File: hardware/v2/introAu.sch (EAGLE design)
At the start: 21 parts

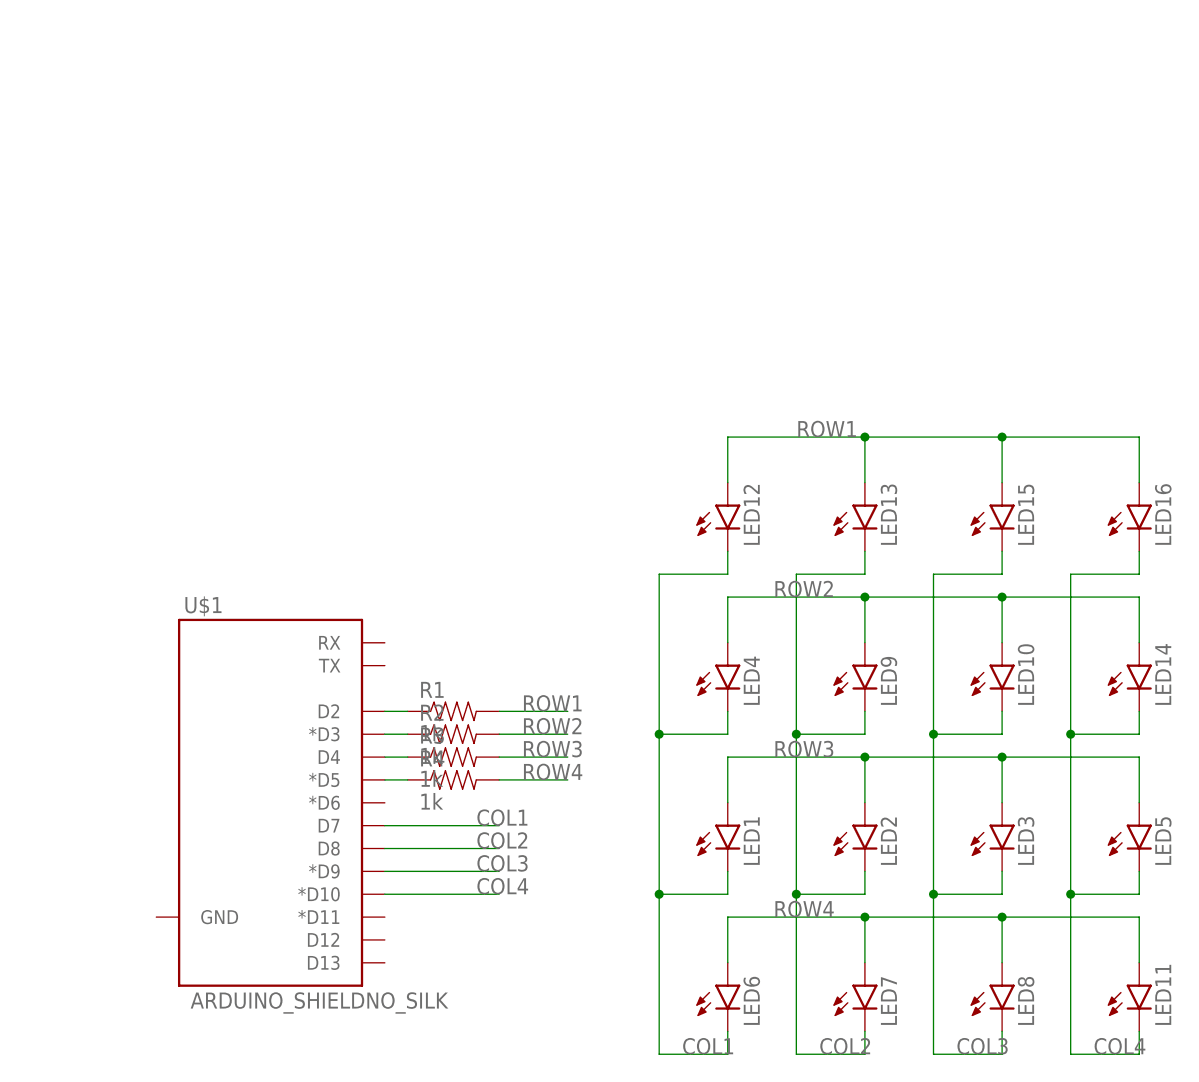
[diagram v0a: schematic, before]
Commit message: Added potentiometer, button, surface mount LEDs to v2
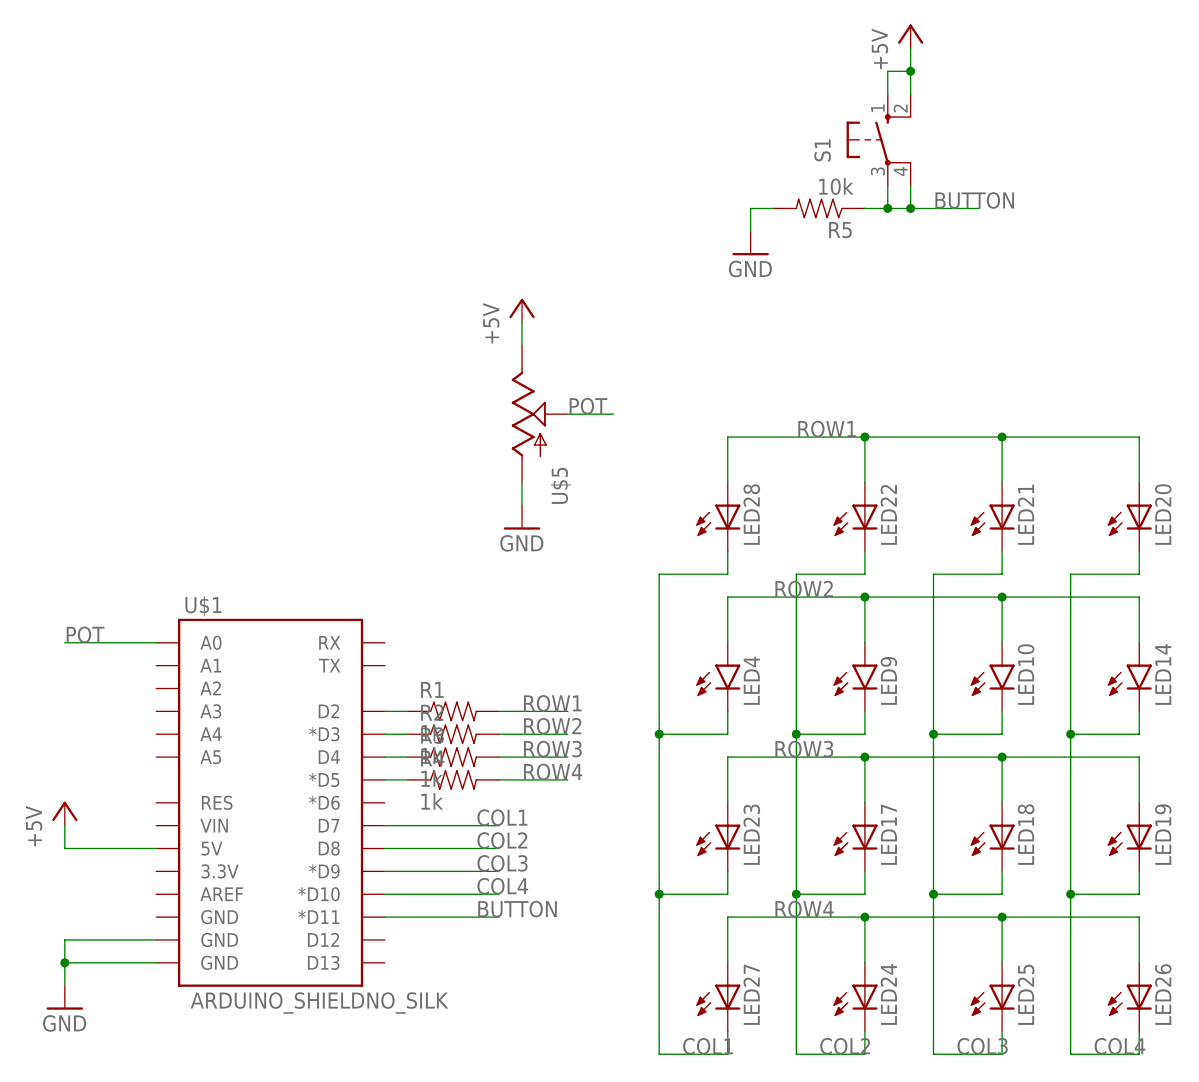
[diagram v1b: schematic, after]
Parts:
- removed LED1, LED11, LED12, LED13, LED15, LED16, LED2, LED3, LED5, LED6, LED7, LED8: (no value), SparkFun-LED:LED5MM
- added LED17, LED18, LED19, LED20, LED21, LED22, LED23, LED24, LED25, LED26, LED27, LED28: (no value), led:LEDCHIPLED_0805
- added R5: 10k, SparkFun-Resistors:1KOHM1/4W5%(PTH)HORIZ-KIT
- added S1: (no value), MESH_Arduino:TACT_BUTTON
- added U$5: (no value), SparkFun-Electromechanical:POT
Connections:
- new net +5V: S1.S, S1.S1, U$1.5V, U$5.E
- new net BUTTON: R5.1, S1.P, S1.P1, U$1.*D11
- new net GND: R5.2, U$1.GND@0, U$1.GND@1, U$5.A
- new net POT: U$1.A0, U$5.S
- net COL1: now also LED23.C, LED27.C, LED28.C; no longer LED1.C, LED12.C, LED6.C
- net COL2: now also LED17.C, LED22.C, LED24.C; no longer LED13.C, LED2.C, LED7.C
- net COL3: now also LED18.C, LED21.C, LED25.C; no longer LED15.C, LED3.C, LED8.C
- net COL4: now also LED19.C, LED20.C, LED26.C; no longer LED11.C, LED16.C, LED5.C
- net ROW1: now also LED20.A, LED21.A, LED22.A, LED28.A; no longer LED12.A, LED13.A, LED15.A, LED16.A
- net ROW3: now also LED17.A, LED18.A, LED19.A, LED23.A; no longer LED1.A, LED2.A, LED3.A, LED5.A
- net ROW4: now also LED24.A, LED25.A, LED26.A, LED27.A; no longer LED11.A, LED6.A, LED7.A, LED8.A

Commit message: Merged in Leonardo onboard
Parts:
- removed R3, R4: 1k, SparkFun-Resistors:1KOHM1/4W5%(PTH)HORIZ-KIT
- removed U$1: ARDUINO_SHIELDNO_SILK, SparkFun-Boards:ARDUINO_SHIELDNO_SILK
- added C1, C2: 100nF, rcl:C-EUC0805
- added JP1, JP2: (no value), SparkFun-Connectors:M06SMD-STRAIGHT-COMBO
- added JP3, JP4: (no value), SparkFun-Connectors:M08SMD-COMBO
- added JP5: (no value), SparkFun-Connectors:M03X22X3_SILK_SM
- added L1: (no value), EagleLibrary_Wuerth_Elektronik_eiSos_rev15c:WE-CBF_0805(WB/HS)
- added LED1: (no value), led:LEDCHIPLED_0805
- added Q1: CERAMIC_RESONATOR_SMD6M00G53Z, MESH_Arduino:CERAMIC_RESONATOR_SMD6M00G53Z
- added R10, R8, R9: 1k, rcl:R-US_R0805
- added R6, R7: 22, rcl:R-US_R0805
- added U$2: ATMEGA32U4TQFP, SparkFun-DigitalIC:ATMEGA32U4TQFP
- added U$3: USB_MICROB_0001LF, mBLE:USB_MICROB_0001LF
- added Z1: zenor 3.6w, rcl:R-EU_R0603
- added Z2: zener 3.6w, rcl:R-EU_R0603
- R1: device SparkFun-Resistors:1KOHM1/4W5%(PTH)HORIZ-KIT -> rcl:R-US_R0805
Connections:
- removed net N$16: R1.1, U$1.D2
- removed net N$17: R2.1, U$1.*D3
- removed net N$18: R3.1, U$1.D4
- removed net N$19: R4.1, U$1.*D5
- new net +3V3: JP2.2
- new net A0: JP1.1
- new net A1: JP1.2, U$2.PF6(ADC6)
- new net A2: JP1.3, U$2.PF5(ADC5)
- new net A3: JP1.4, U$2.PF4(ADC4)
- new net A4: JP1.5, U$2.PF1(ADC1)
- new net A5: JP1.6, U$2.PF0(ADC0)
- new net AREF: C2.1, JP4.1, L1.2, U$2.AREF
- new net D0: JP3.8, U$2.PD2(RX)
- new net D1: JP3.7, U$2.PD3(TX)
- new net D10: JP4.6
- new net D11: JP4.5, U$2.PB7
- new net D12: JP4.4, U$2.PD6(ADC9)
- new net D13: JP4.3, U$2.PC7
- new net D14: U$2.PB3(MISO)
- new net D15: U$2.PB1(SCK)
- new net D16: U$2.PB2(MOSI)
- new net D17: U$2.PB0(SS)
- new net D2: JP3.6
- new net D3: JP3.5
- new net D4: JP3.4
- new net D5: JP3.3
- new net D6: JP3.2
- new net D7: JP3.1
- new net D8: JP4.8
- new net D9: JP4.7
- new net MISO: JP5.1
- new net MOSI: JP5.4
- new net N$1: R10.1, U$2.PD1(SDA)
- new net N$11: LED1.A, R1.1
- new net N$2: R2.1, U$2.PD0(SCL)
- new net N$3: R9.1, U$2.PD4(ADC8)
- new net N$4: R8.1, U$2.PC6
- new net N$5: Q1.3, U$2.XTAL2
- new net N$6: Q1.1, U$2.XTAL1
- new net N$7: R7.1, U$3.D-, Z2.2
- new net N$9: R6.1, U$3.D+, Z1.2
- new net RD+: R6.2, U$2.D+
- new net RD-: R7.2, U$2.D-
- new net RESET: JP2.1, JP5.5, U$2.!RESET
- new net SCK: JP5.3
- new net TX: U$2.PD5
- new net VIN: JP2.6
- net +5V: now also C1.1, JP2.3, JP5.2, L1.1, R1.2, U$2.AVCC@24, U$2.AVCC@44, U$2.UVCC, U$2.VBUS, U$2.VCC@14, U$2.VCC@34, U$3.+5V; no longer U$1.5V
- net BUTTON: now also U$2.PB6(ADC13); no longer U$1.*D11
- net COL1: now also U$2.PD7(ADC10); no longer U$1.D7
- net COL2: now also U$2.PE6; no longer U$1.D8
- net COL3: now also U$2.PB4(ADC11); no longer U$1.*D9
- net COL4: now also U$2.PB5(ADC12); no longer U$1.*D10
- net GND: now also C1.2, C2.2, JP2.4, JP2.5, JP4.2, JP5.6, LED1.C, Q1.2, U$2.GND@15, U$2.GND@23, U$2.GND@35, U$2.GND@43, U$2.UCAP, U$2.UGND, U$3.GND, Z1.1, Z2.1; no longer U$1.GND@0, U$1.GND@1
- net POT: now also U$2.PF7(ADC7); no longer U$1.A0
- net ROW1: now also R10.2; no longer R1.2
- net ROW3: now also R9.2; no longer R3.2
- net ROW4: now also R8.2; no longer R4.2
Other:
- note added: "POWER LED"
- moved on the sheet: R1, R2
